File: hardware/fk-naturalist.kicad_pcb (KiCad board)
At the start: 2 copper layers, 106 x 37 mm, 140 parts, among them J1 Conn_01x11, J10 S2B-PH-SM4-TB, J11 RF-SMA-EDGE, J2 Conn_01x05, J3 Conn_01x04, J5 Conn_01x03, J6 Conn_01x05, J7 CONN-HDR-2x5, J8 Conn_01x09, J9 MICRO-USB, M1 MOUNT_HOLE, M3 MOUNT_HOLE, M4 MOUNT_HOLE, M6 MOUNT_HOLE, M7 MICROSD, Q1 2N7002LT1G, Q2 2N7002LT1G, Q3 2N7002LT1G, Q4 2N7002LT1G, SW1 SPNO, SW2 SPNO, U1 ATWINC1500-MR210PA, U10 FGPMMOPA6H, U101 TSL2591, U102 MPL3115A2, U103 BNO055, U104 SHT31, U11 MAX1704XX, U2 ATSAMD21G18A-AU, U3 SPH0645, U4 24AA02E64, U5 S25FL116K0XMFI041, U6 BQ24074RGTT, U7 PCF8523, U8 MCP1700T-3302E/MB, U9 ISL8541x, Y1 FC-135, Y101 FC-135, Y2 FC-135

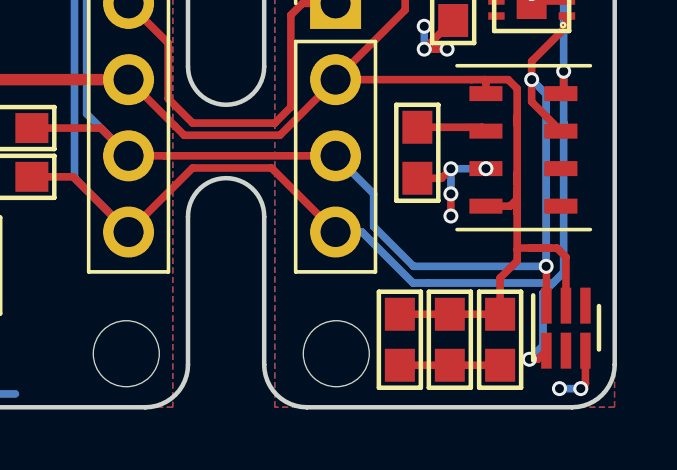
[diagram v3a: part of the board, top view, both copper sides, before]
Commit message: Nudge some passives away from a sensor.
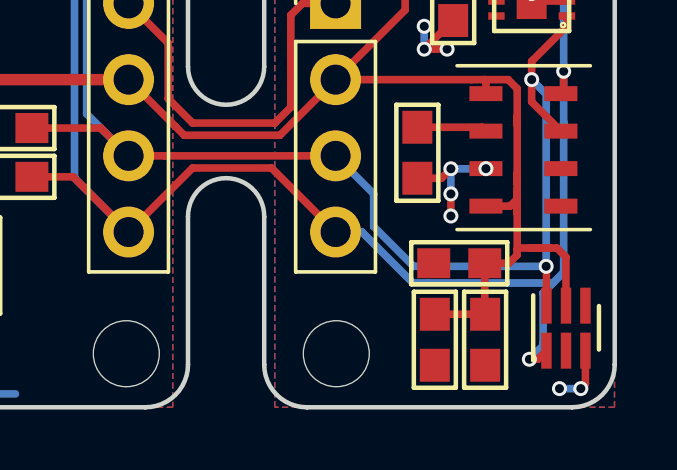
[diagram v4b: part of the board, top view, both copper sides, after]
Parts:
- moved C101 3.23 mm to (178.2, 142.0), turned to 180 degrees
- moved C103 0.50 mm to (179.1, 144.6)
- moved C104 0.50 mm to (177.4, 144.6)
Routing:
- net GND: track 107.6 -> 104.3 mm
- net 3V3: track 437.7 -> 436.7 mm
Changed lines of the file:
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@@
     (links 368)
     (no_connects 0)
-    (area 62.463333 95.834285 191.661515 152.064743)
+    (area 62.463333 95.834285 191.661515 151.864743)
     (thickness 1.6)
     (drawings 52)
-    (tracks 1564)
+    (tracks 1563)
     (zones 0)
     (modules 140)
@@
   )
   (module RocketScreamKicadLibrary:CAP-0603 (layer F.Cu)
-    (at 176.226271 144.560263 270)
+    (at 178.2064 142.0114 180)
     (descr "Capacitor SMD 0603")
     (tags "capacitor 0603")
     (attr smd)
-    (fp_text reference C101 (at 0 -1.9 270) (layer F.SilkS) hide
+    (fp_text reference C101 (at 0 -1.9 180) (layer F.SilkS) hide
       (effects (font (size 1 1) (thickness 0.15)))
     )
-    (fp_text value 1uF (at 3.255037 -0.075129 270) (layer F.Fab)
+    (fp_text value 1uF (at 3.255037 -0.075129 180) (layer F.Fab)
       (effects (font (size 1 1) (thickness 0.15)))
     )
@@
     (fp_line (start -1.6 -0.7) (end 1.6 -0.7) (layer F.SilkS) (width 0.15))
     (fp_line (start 1.6 0.7) (end -1.6 0.7) (layer F.SilkS) (width 0.15))
-    (pad 1 smd rect (at -0.85 0 270) (size 1.1 1) (layers F.Cu F.Paste F.Mask)
+    (pad 1 smd rect (at -0.85 0 180) (size 1.1 1) (layers F.Cu F.Paste F.Mask)
       (net 2 3V3))
-    (pad 2 smd rect (at 0.85 0 270) (size 1.1 1) (layers F.Cu F.Paste F.Mask)
+    (pad 2 smd rect (at 0.85 0 180) (size 1.1 1) (layers F.Cu F.Paste F.Mask)
       (net 1 GND))
     (model RocketScreamKicadLibrary.3dshapes/CAP-0603.wrl
@@
   )
   (module RocketScreamKicadLibrary:CAP-0603 (layer F.Cu)
-    (at 179.567982 144.560263 270)
+    (at 179.067982 144.560263 270)
     (descr "Capacitor SMD 0603")
     (tags "capacitor 0603")
@@
   )
   (module RocketScreamKicadLibrary:CAP-0603 (layer F.Cu)
-    (at 177.891582 144.560263 270)
+    (at 177.391582 144.560263 270)
     (descr "Capacitor SMD 0603")
     (tags "capacitor 0603")
@@
   (segment (start 182.4124 146.035) (end 182.2577 146.1897) (width 0.254) (layer F.Cu) (net 1))
   (via (at 182.2577 146.1897) (size 0.5) (drill 0.3) (layers F.Cu B.Cu) (net 1))
-  (segment (start 176.226271 145.410263) (end 177.891582 145.410263) (width 0.254) (layer F.Cu) (net 1))
-  (segment (start 179.567982 145.410263) (end 177.891582 145.410263) (width 0.254) (layer F.Cu) (net 1))
   (segment (start 101.535319 121.629777) (end 102.360319 121.629777) (width 0.254) (layer F.Cu) (net 1))
   (via (at 102.360319 121.629777) (size 0.5) (drill 0.3) (layers F.Cu B.Cu) (net 1))
@@
   (via (at 81.4324 140.1064) (size 0.5) (drill 0.3) (layers F.Cu B.Cu) (net 1))
   (segment (start 102.244819 127.970777) (end 102.244819 127.920777) (width 0.254) (layer F.Cu) (net 1))
+  (segment (start 179.0564 142.0114) (end 179.8604 142.0114) (width 0.254) (layer F.Cu) (net 2))
+  (segment (start 179.8604 142.0114) (end 180.1368 141.735) (width 0.254) (layer F.Cu) (net 2))
+  (segment (start 180.1368 141.735) (end 180.1368 141.5542) (width 0.254) (layer F.Cu) (net 2))
+  (segment (start 177.391582 143.710263) (end 179.067982 143.710263) (width 0.254) (layer F.Cu) (net 2))
+  (segment (start 179.0564 142.0114) (end 179.0564 143.698681) (width 0.254) (layer F.Cu) (net 2))
+  (segment (start 179.0564 143.698681) (end 179.067982 143.710263) (width 0.254) (layer F.Cu) (net 2))
   (segment (start 95.0976 143.73) (end 95.0976 142.926) (width 0.254) (layer F.Cu) (net 2))
   (segment (start 95.0976 142.926) (end 95.957401 142.066199) (width 0.254) (layer F.Cu) (net 2))
@@
   (segment (start 157.429087 143.175801) (end 160.963799 143.175801) (width 0.254) (layer B.Cu) (net 2))
   (segment (start 160.963799 143.175801) (end 161.036 143.1036) (width 0.254) (layer B.Cu) (net 2))
-  (segment (start 176.226271 143.710263) (end 177.891582 143.710263) (width 0.254) (layer F.Cu) (net 2))
-  (segment (start 179.567982 143.710263) (end 177.891582 143.710263) (width 0.254) (layer F.Cu) (net 2))
-  (segment (start 179.567982 143.710263) (end 179.567982 142.499863) (width 0.254) (layer F.Cu) (net 2))
-  (segment (start 179.567982 142.499863) (end 180.1368 141.931045) (width 0.254) (layer F.Cu) (net 2))
-  (segment (start 180.1368 141.931045) (end 180.1368 141.5542) (width 0.254) (layer F.Cu) (net 2))
   (segment (start 167.1828 118.11) (end 168.032799 118.959999) (width 0.254) (layer F.Cu) (net 2))
   (segment (start 168.032799 118.959999) (end 168.032799 119.828485) (width 0.254) (layer F.Cu) (net 2))
@@
     (connect_pads (clearance 0.2032))
     (min_thickness 0.2032)
-    (fill yes (arc_segments 32) (thermal_gap 0.254) (thermal_bridge_width 0.254))
+    (fill (arc_segments 32) (thermal_gap 0.254) (thermal_bridge_width 0.254))
     (polygon
       (pts
@@
     (connect_pads (clearance 0.2032))
     (min_thickness 0.2032)
-    (fill yes (arc_segments 32) (thermal_gap 0.254) (thermal_bridge_width 0.254))
+    (fill (arc_segments 32) (thermal_gap 0.254) (thermal_bridge_width 0.254))
     (polygon
       (pts
@@
     (connect_pads (clearance 0.2032))
     (min_thickness 0.2032)
-    (fill yes (arc_segments 32) (thermal_gap 0.254) (thermal_bridge_width 0.254))
+    (fill (arc_segments 32) (thermal_gap 0.254) (thermal_bridge_width 0.254))
     (polygon
       (pts
@@
     (connect_pads (clearance 0.2032))
     (min_thickness 0.2032)
-    (fill yes (arc_segments 32) (thermal_gap 0.254) (thermal_bridge_width 0.254))
+    (fill (arc_segments 32) (thermal_gap 0.254) (thermal_bridge_width 0.254))
     (polygon
       (pts
@@
     (connect_pads (clearance 0.2032))
     (min_thickness 0.2032)
-    (fill yes (arc_segments 32) (thermal_gap 0.254) (thermal_bridge_width 0.254))
+    (fill (arc_segments 32) (thermal_gap 0.254) (thermal_bridge_width 0.254))
     (polygon
       (pts
@@
     (connect_pads (clearance 0.2032))
     (min_thickness 0.2032)
-    (fill yes (arc_segments 32) (thermal_gap 0.254) (thermal_bridge_width 0.254))
+    (fill (arc_segments 32) (thermal_gap 0.254) (thermal_bridge_width 0.254))
     (polygon
       (pts
@@
     (connect_pads (clearance 0.2032))
     (min_thickness 0.2032)
-    (fill yes (arc_segments 32) (thermal_gap 0.254) (thermal_bridge_width 0.254))
+    (fill (arc_segments 32) (thermal_gap 0.254) (thermal_bridge_width 0.254))
     (polygon
       (pts
@@
     (connect_pads (clearance 0.2032))
     (min_thickness 0.2032)
-    (fill yes (arc_segments 32) (thermal_gap 0.254) (thermal_bridge_width 0.254))
+    (fill (arc_segments 32) (thermal_gap 0.254) (thermal_bridge_width 0.254))
     (polygon
       (pts
@@
     (connect_pads (clearance 0.2032))
     (min_thickness 0.2032)
-    (fill yes (arc_segments 32) (thermal_gap 0.254) (thermal_bridge_width 0.254))
+    (fill (arc_segments 32) (thermal_gap 0.254) (thermal_bridge_width 0.254))
     (polygon
       (pts
@@
     (connect_pads (clearance 0.2032))
     (min_thickness 0.2032)
-    (fill yes (arc_segments 32) (thermal_gap 0.254) (thermal_bridge_width 0.254))
+    (fill (arc_segments 32) (thermal_gap 0.254) (thermal_bridge_width 0.254))
     (polygon
       (pts
